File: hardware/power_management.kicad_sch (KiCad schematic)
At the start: 7 parts, among them Q1 IRLML6402, U2 BMS Module

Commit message: added footprint to test points
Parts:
- TP16, TP17: footprint (none) -> TestPoint:TestPoint_Pad_D2.0mm
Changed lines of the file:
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@@
 			)
 		)
-		(property "Footprint" ""
+		(property "Footprint" "TestPoint:TestPoint_Pad_D2.0mm"
 			(at 127 113.03 0)
 			(effects
@@
 			)
 		)
-		(property "Footprint" ""
+		(property "Footprint" "TestPoint:TestPoint_Pad_D2.0mm"
 			(at 127 115.57 0)
 			(effects

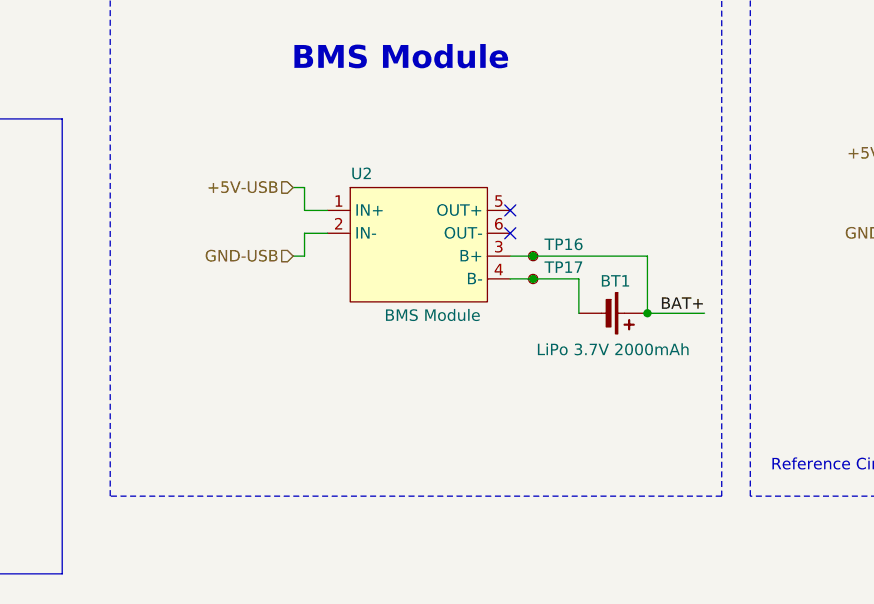
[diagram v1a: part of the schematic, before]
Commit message: Removed comments on UART, added some footprints and started fixing rule checks
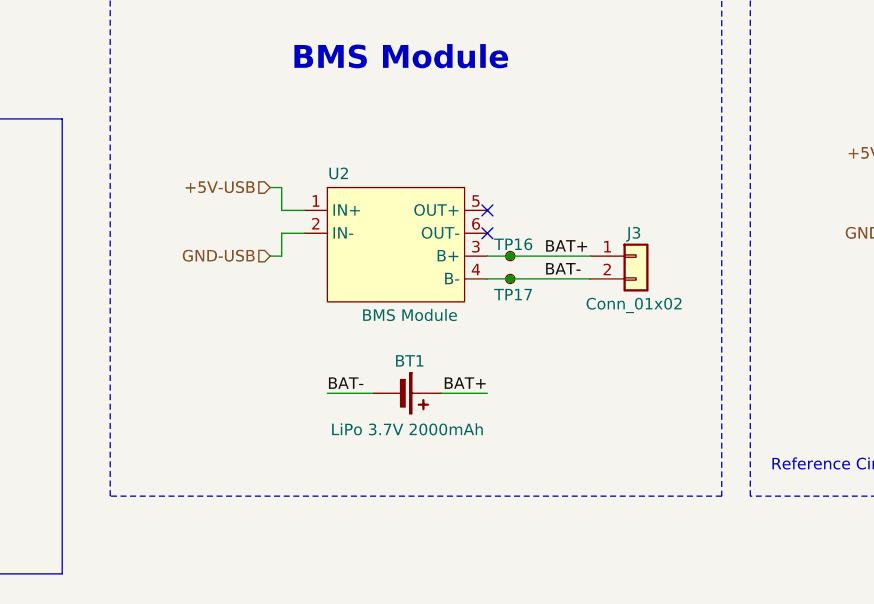
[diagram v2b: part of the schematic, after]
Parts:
- added J3: Conn_01x02, kitchen_timer:JST_XH_1x02_P2.54mm_Vertical, symbol Connector_Generic:Conn_01x02
- BT1: now left out of the parts list
- D3: Manuf. Name (none) -> Nexperia; Manuf. Part # (none) -> PMEG4010CEJ,115; Part Num PMEG4010CEJ,115 -> (none); Price/unit $0.0699 -> (none); Supplier Name (none) -> JLCPCB; Supplier Part # (none) -> C50704; Supplier Unit Price (none) -> $0.0699
- Q1: Manuf. Name (none) -> Infineon Technologies; Manuf. Part # (none) -> IRLML6402TRPBF; Part Num IRLML6402TRPBF -> (none); Price/unit $0.0906 -> (none); Supplier Name (none) -> JLCPCB; Supplier Part # (none) -> C2593; Supplier Unit Price (none) -> $0.0906
- R4: footprint (none) -> Resistor_SMD:R_0805_2012Metric_Pad1.20x1.40mm_HandSolder; Manuf. Name (none) -> UNI-ROYAL(Uniroyal Elec); Manuf. Part # (none) -> 0805W8F1002T5E; Part Num 0805W8F1002T5E -> (none); Price/unit $0.0017 -> (none); Supplier Name (none) -> JLCPCB; Supplier Part # (none) -> C17414; Supplier Unit Price (none) -> $0.0017
- U2: footprint (none) -> kitchen_timer:TP4056_BREAKOUT; Manuf. Name (none) -> Unknown; Manuf. Part # (none) -> TP4056; Part Num TP4056 -> NA; Price/unit 45 kr -> (none); Supplier Name (none) -> ELECTROKIT; Supplier Part # (none) -> 41018444; Supplier Unit Price (none) -> 45 kr
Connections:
- net BAT+: now also J3.1 (Pin_1)
- net BAT-: now reaches BT1.2 (-), TP17.1, U2.4 (B-)
- net BAT-: now also J3.2 (Pin_2)
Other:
- moved on the sheet: BT1, TP16, TP17, U2

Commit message: Added switch footprint, SparkFun_LiPower footprint
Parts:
- J3, U2: now left out of the parts list
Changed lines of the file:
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@@
 		(unit 1)
 		(exclude_from_sim no)
-		(in_bom yes)
+		(in_bom no)
 		(on_board yes)
 		(dnp no)
@@
 		(unit 1)
 		(exclude_from_sim no)
-		(in_bom yes)
+		(in_bom no)
 		(on_board yes)
 		(dnp no)

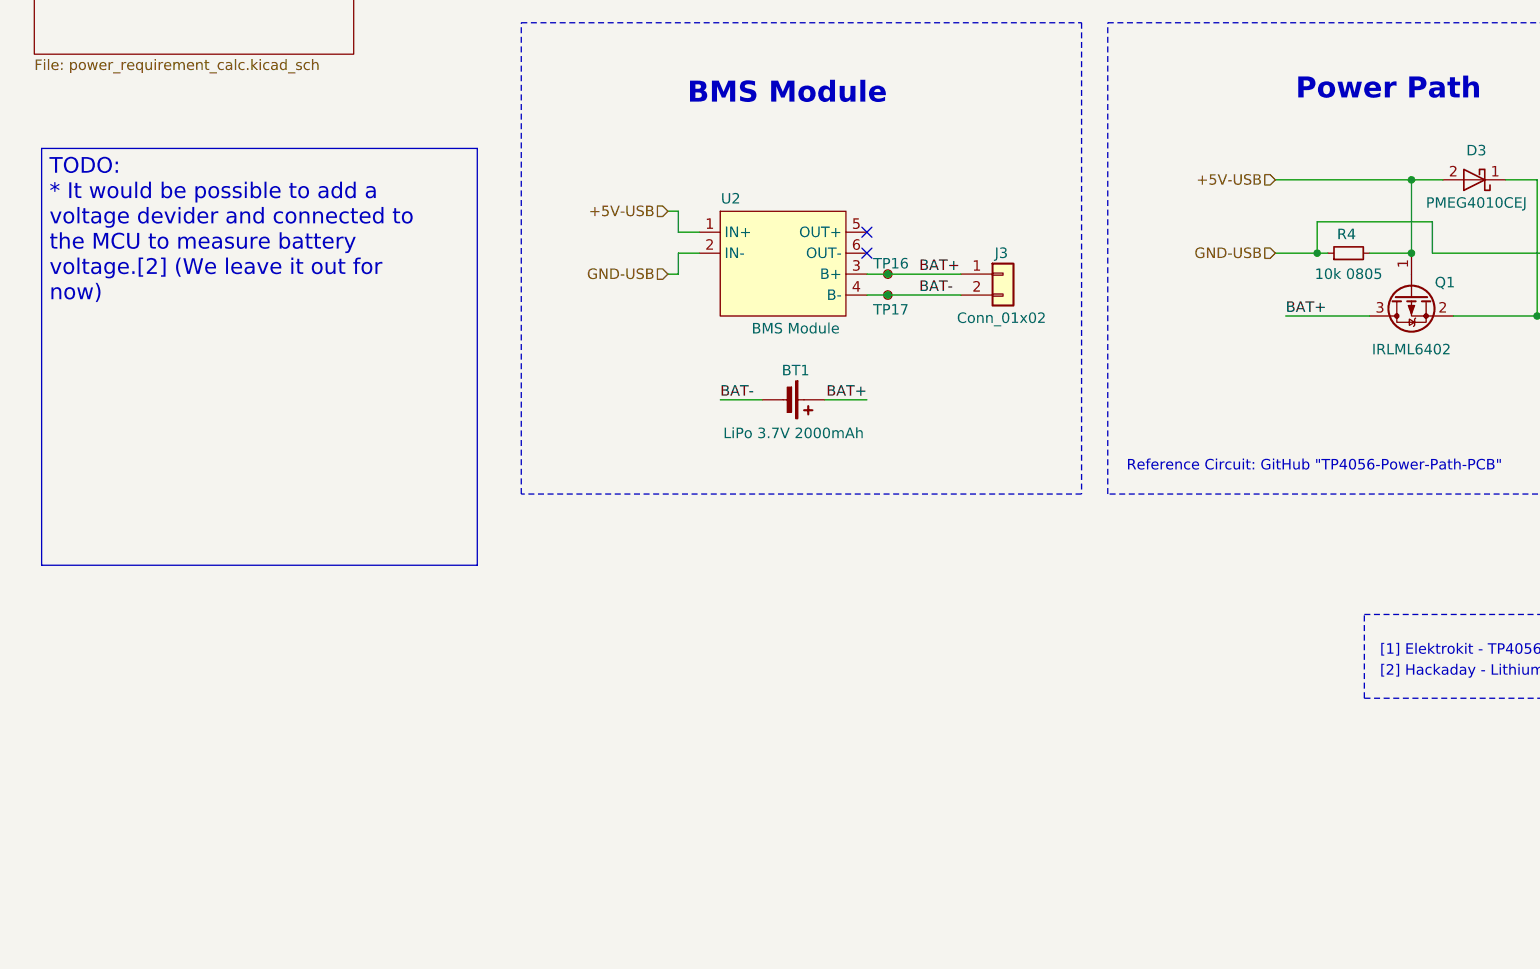
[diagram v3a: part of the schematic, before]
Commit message: Added many footprints and populated part of the property tables
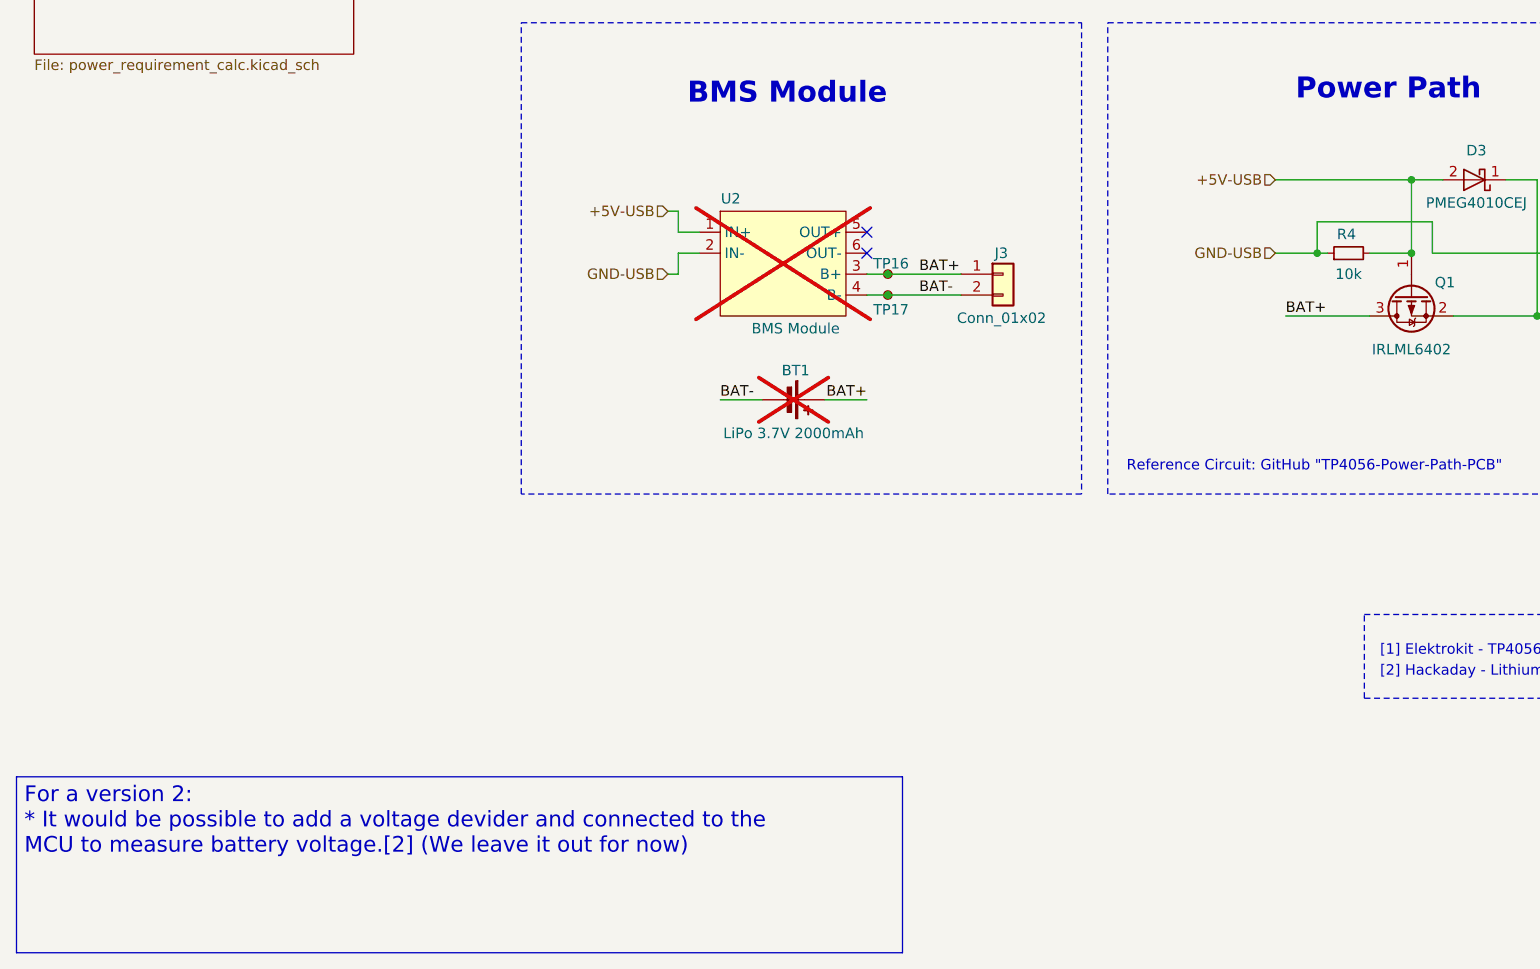
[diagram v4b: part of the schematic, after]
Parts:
- BT1: footprint (none) -> ~; now not fitted
- D3: Supplier Unit Price $0.0699 -> $0.0612
- J3: Supplier Unit Price 0.00 -> (none)
- Q1: Supplier Unit Price $0.0906 -> $0.0795
- R4: value 10k 0805 -> 10k; Manuf. Name UNI-ROYAL(Uniroyal Elec) -> UNI-ROYAL(Uniroyal Elec)
- U2: now not fitted
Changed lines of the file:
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@@
 		)
 	)
-	(text_box "TODO:\n* It would be possible to add a voltage devider and connected to the MCU to measure battery voltage.[2] (We leave it out for now)\n"
+	(text_box "For a version 2:\n* It would be possible to add a voltage devider and connected to the MCU to measure battery voltage.[2] (We leave it out for now)\n"
 		(exclude_from_sim no)
-		(at 16.764 97.79 0)
-		(size 52.832 50.546)
+		(at 13.716 173.99 0)
+		(size 107.442 21.336)
 		(margins 0.9525 0.9525 0.9525 0.9525)
 		(stroke
 			(width 0)
 			(type solid)
-			(color 194 0 0 1)
+			(color 0 0 132 1)
 		)
 		(fill
@@
 			(font
 				(size 1.905 1.905)
-				(color 194 0 0 1)
+				(color 0 0 132 1)
 			)
 			(justify left top)
@@
 			)
 		)
-		(property "Datasheet" "https://www.lcsc.com/datasheet/lcsc_datasheet_1809291616_Nexperia-PMEG4010CEJ-115_C50704.pdf"
+		(property "Datasheet" "https://jlcpcb.com/api/file/downloadByFileSystemAccessId/8586185406685851648"
 			(at 190.5 101.6 0)
 			(effects
@@
 			)
 		)
-		(property "Supplier Unit Price" "$0.0699"
+		(property "Supplier Unit Price" " $0.0612"
 			(at 190.5 101.6 0)
 			(effects
@@
 			)
 		)
-		(property "Value" "10k 0805"
+		(property "Value" "10k"
 			(at 175.26 113.03 90)
 			(effects
@@
 			)
 		)
-		(property "Description" "10k resistor, 0805"
+		(property "Description" "Resistor, small symbol"
 			(at 175.26 110.49 0)
 			(effects
@@
 			)
 		)
-		(property "Manuf. Name" " UNI-ROYAL(Uniroyal Elec)"
+		(property "Manuf. Name" "UNI-ROYAL(Uniroyal Elec)"
 			(at 175.26 110.49 0)
 			(effects
@@
 			)
 		)
-		(property "Supplier Unit Price" "$0.0906"
+		(property "Supplier Unit Price" " $0.0795"
 			(at 182.88 115.57 0)
 			(effects
@@
 			)
 		)
-		(property "Supplier Unit Price" "0.00"
+		(property "Supplier Unit Price" "~"
 			(at 133.35 113.03 0)
 			(effects
@@
 		(in_bom no)
 		(on_board no)
-		(dnp no)
+		(dnp yes)
 		(property "Reference" "BT1"
 			(at 108.204 124.714 90)
@@
 			)
 		)
-		(property "Footprint" ""
+		(property "Footprint" "~"
 			(at 108.204 128.27 90)
 			(effects
@@
 			)
 		)
-		(property "Supplier Link" ""
+		(property "Supplier Link" "~"
 			(at 106.68 128.27 0)
 			(effects
@@
 			)
 		)
-		(property "Package" ""
+		(property "Package" "~"
 			(at 106.68 128.27 0)
 			(effects
@@
 			)
 		)
-		(property "Supplier Name" ""
+		(property "Supplier Name" "~"
 			(at 106.68 128.27 0)
 			(effects
@@
 			)
 		)
-		(property "Supplier Unit Price" ""
+		(property "Supplier Unit Price" "~"
 			(at 106.68 128.27 0)
 			(effects
@@
 			)
 		)
-		(property "Manuf. Name" ""
+		(property "Manuf. Name" "~"
 			(at 106.68 128.27 0)
 			(effects
@@
 			)
 		)
-		(property "Manuf. Part #" ""
+		(property "Manuf. Part #" "~"
 			(at 106.68 128.27 0)
 			(effects
@@
 			)
 		)
-		(property "Supplier Part #" ""
+		(property "Supplier Part #" "~"
 			(at 106.68 128.27 0)
 			(effects
@@
 		(in_bom no)
 		(on_board yes)
-		(dnp no)
+		(dnp yes)
 		(property "Reference" "U2"
 			(at 100.33 103.886 0)

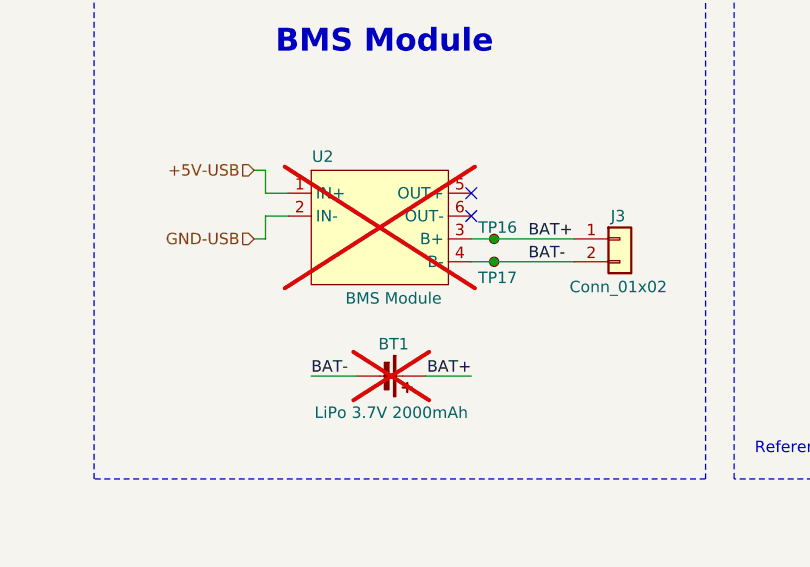
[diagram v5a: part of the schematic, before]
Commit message: Made some small changes on the properties of some components while having last weeks meeting and added the fp-info-cache to the gitignore file
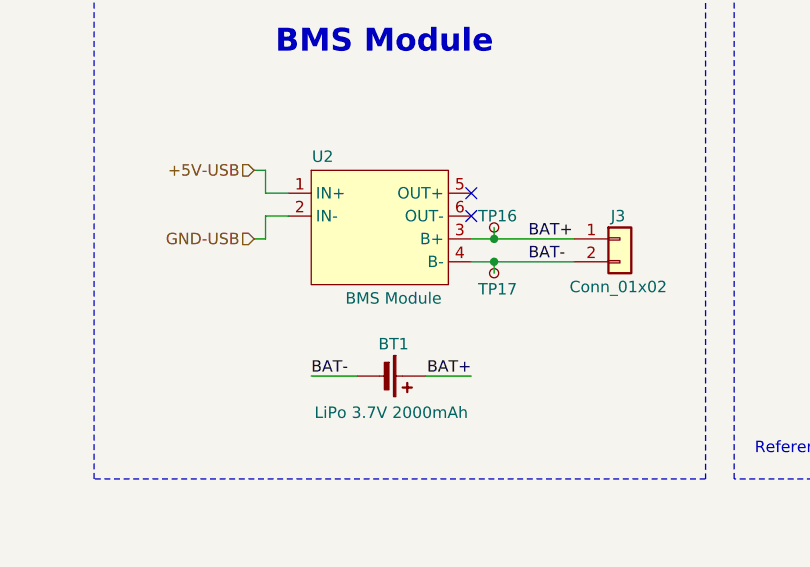
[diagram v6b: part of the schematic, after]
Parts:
- BT1, U2: now fitted
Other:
- moved on the sheet: TP16, TP17
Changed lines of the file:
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@@
+	)
+	(junction
+		(at 119.38 113.03)
+		(diameter 0)
+		(color 0 0 0 0)
+	)
+	(junction
+		(at 182.88 101.6)
+		(diameter 0)
+		(color 0 0 0 0)
+	)
+	(junction
+		(at 171.45 110.49)
+		(diameter 0)
+		(color 0 0 0 0)
 	)
 	(junction
@@
 	)
 	(junction
-		(at 182.88 101.6)
-		(diameter 0)
-		(color 0 0 0 0)
-	)
-	(junction
-		(at 119.38 113.03)
-		(diameter 0)
-		(color 0 0 0 0)
-	)
-	(junction
-		(at 171.45 110.49)
-		(diameter 0)
-		(color 0 0 0 0)
-	)
-	(junction
 		(at 198.12 118.11)
 		(diameter 0)
@@
 	(wire
 		(pts
+			(xy 119.38 115.57) (xy 128.27 115.57)
+		)
+		(stroke
+			(width 0)
+			(type default)
+		)
+	)
+	(wire
+		(pts
 			(xy 198.12 118.11) (xy 200.66 118.11)
 		)
@@
 	(wire
 		(pts
+			(xy 119.38 111.76) (xy 119.38 113.03)
+		)
+		(stroke
+			(width 0)
+			(type default)
+		)
+	)
+	(wire
+		(pts
+			(xy 119.38 113.03) (xy 128.27 113.03)
+		)
+		(stroke
+			(width 0)
+			(type default)
+		)
+	)
+	(wire
+		(pts
 			(xy 116.84 115.57) (xy 119.38 115.57)
 		)
@@
 	(wire
 		(pts
-			(xy 119.38 113.03) (xy 128.27 113.03)
+			(xy 116.84 113.03) (xy 119.38 113.03)
 		)
 		(stroke
@@
 	(wire
 		(pts
+			(xy 119.38 115.57) (xy 119.38 116.84)
+		)
+		(stroke
+			(width 0)
+			(type default)
+		)
+	)
+	(wire
+		(pts
 			(xy 187.96 118.11) (xy 198.12 118.11)
 		)
@@
 	(wire
 		(pts
-			(xy 116.84 113.03) (xy 119.38 113.03)
-		)
-		(stroke
-			(width 0)
-			(type default)
-		)
-	)
-	(wire
-		(pts
 			(xy 185.42 110.49) (xy 200.66 110.49)
 		)
@@
 		(pts
 			(xy 93.98 110.49) (xy 96.52 110.49)
-		)
-		(stroke
-			(width 0)
-			(type default)
-		)
-	)
-	(wire
-		(pts
-			(xy 119.38 115.57) (xy 128.27 115.57)
 		)
 		(stroke
@@
 	(symbol
 		(lib_id "Connector:TestPoint_Small")
-		(at 119.38 113.03 0)
+		(at 119.38 111.76 0)
 		(unit 1)
 		(exclude_from_sim no)
@@
 		(dnp no)
 		(property "Reference" "TP16"
-			(at 117.602 111.76 0)
+			(at 117.602 110.49 0)
 			(effects
 				(font
@@
 		)
 		(property "Value" "TestPoint"
-			(at 119.126 109.474 0)
+			(at 119.126 108.204 0)
 			(effects
 				(font
@@
 		)
 		(property "Footprint" "TestPoint:TestPoint_Pad_D2.0mm"
-			(at 124.46 113.03 0)
+			(at 124.46 111.76 0)
 			(effects
 				(font
@@
 		)
 		(property "Datasheet" "~"
-			(at 124.46 113.03 0)
+			(at 124.46 111.76 0)
 			(effects
 				(font
@@
 		)
 		(property "Description" "Test Point, 2.0mm"
-			(at 119.38 113.03 0)
+			(at 119.38 111.76 0)
 			(effects
 				(font
@@
 		)
 		(property "Supplier Name" "~"
-			(at 119.38 113.03 0)
+			(at 119.38 111.76 0)
 			(effects
 				(font
@@
 		)
 		(property "Manuf. Name" "~"
-			(at 119.38 113.03 0)
-			(effects
-				(font
-					(size 1.27 1.27)
-				)
+			(at 119.38 111.76 0)
+			(effects
+				(font
+					(size 1.27 1.27)
+				)
+				(hide yes)
 			)
 		)
 		(property "Manuf. Part #" "~"
-			(at 119.38 113.03 0)
-			(effects
-				(font
-					(size 1.27 1.27)
-				)
+			(at 119.38 111.76 0)
+			(effects
+				(font
+					(size 1.27 1.27)
+				)
+				(hide yes)
 			)
 		)
 		(property "Supplier Link" "~"
-			(at 119.38 113.03 0)
-			(effects
-				(font
-					(size 1.27 1.27)
-				)
+			(at 119.38 111.76 0)
+			(effects
+				(font
+					(size 1.27 1.27)
+				)
+				(hide yes)
 			)
 		)
 		(property "Supplier Part #" "~"
-			(at 119.38 113.03 0)
-			(effects
-				(font
-					(size 1.27 1.27)
-				)
+			(at 119.38 111.76 0)
+			(effects
+				(font
+					(size 1.27 1.27)
+				)
+				(hide yes)
 			)
 		)
 		(property "Supplier Unit Price" "~"
-			(at 119.38 113.03 0)
-			(effects
-				(font
-					(size 1.27 1.27)
-				)
+			(at 119.38 111.76 0)
+			(effects
+				(font
+					(size 1.27 1.27)
+				)
+				(hide yes)
 			)
 		)
@@
 		(in_bom no)
 		(on_board no)
-		(dnp yes)
+		(dnp no)
 		(property "Reference" "BT1"
 			(at 108.204 124.714 90)
@@
 	(symbol
 		(lib_id "Connector:TestPoint_Small")
-		(at 119.38 115.57 0)
+		(at 119.38 116.84 0)
 		(unit 1)
 		(exclude_from_sim no)
@@
 		(dnp no)
 		(property "Reference" "TP17"
-			(at 117.602 117.348 0)
+			(at 117.602 118.618 0)
 			(effects
 				(font
@@
 		)
 		(property "Value" "TestPoint"
-			(at 119.126 112.014 0)
+			(at 119.126 113.284 0)
 			(effects
 				(font
@@
 		)
 		(property "Footprint" "TestPoint:TestPoint_Pad_D2.0mm"
-			(at 124.46 115.57 0)
+			(at 124.46 116.84 0)
 			(effects
 				(font
@@
 		)
 		(property "Datasheet" "~"
-			(at 124.46 115.57 0)
+			(at 124.46 116.84 0)
 			(effects
 				(font
@@
 		)
 		(property "Description" "Test Point, 2.0mm"
-			(at 119.38 115.57 0)
+			(at 119.38 116.84 0)
 			(effects
 				(font
@@
 		)
 		(property "Supplier Name" "~"
-			(at 119.38 115.57 0)
+			(at 119.38 116.84 0)
 			(effects
 				(font
@@
 		)
 		(property "Manuf. Name" "~"
-			(at 119.38 115.57 0)
-			(effects
-				(font
-					(size 1.27 1.27)
-				)
+			(at 119.38 116.84 0)
+			(effects
+				(font
+					(size 1.27 1.27)
+				)
+				(hide yes)
 			)
 		)
 		(property "Manuf. Part #" "~"
-			(at 119.38 115.57 0)
-			(effects
-				(font
-					(size 1.27 1.27)
-				)
+			(at 119.38 116.84 0)
+			(effects
+				(font
+					(size 1.27 1.27)
+				)
+				(hide yes)
 			)
 		)
 		(property "Supplier Link" "~"
-			(at 119.38 115.57 0)
-			(effects
-				(font
-					(size 1.27 1.27)
-				)
+			(at 119.38 116.84 0)
+			(effects
+				(font
+					(size 1.27 1.27)
+				)
+				(hide yes)
 			)
 		)
 		(property "Supplier Part #" "~"
-			(at 119.38 115.57 0)
-			(effects
-				(font
-					(size 1.27 1.27)
-				)
+			(at 119.38 116.84 0)
+			(effects
+				(font
+					(size 1.27 1.27)
+				)
+				(hide yes)
 			)
 		)
 		(property "Supplier Unit Price" "~"
-			(at 119.38 115.57 0)
-			(effects
-				(font
-					(size 1.27 1.27)
-				)
+			(at 119.38 116.84 0)
+			(effects
+				(font
+					(size 1.27 1.27)
+				)
+				(hide yes)
 			)
 		)
@@
 		(in_bom no)
 		(on_board yes)
-		(dnp yes)
+		(dnp no)
 		(property "Reference" "U2"
 			(at 100.33 103.886 0)
